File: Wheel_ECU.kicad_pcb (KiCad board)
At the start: 2 copper layers, 61 x 61 mm, 61 parts, among them J1 Conn_01x04, J2 Conn_01x04, J3 Conn_01x02, J4 Debug, J5 Conn_01x02, U1 IFX9201SG, U2 TLE4964, U3 XMC1404_F064, U4 TLE7251

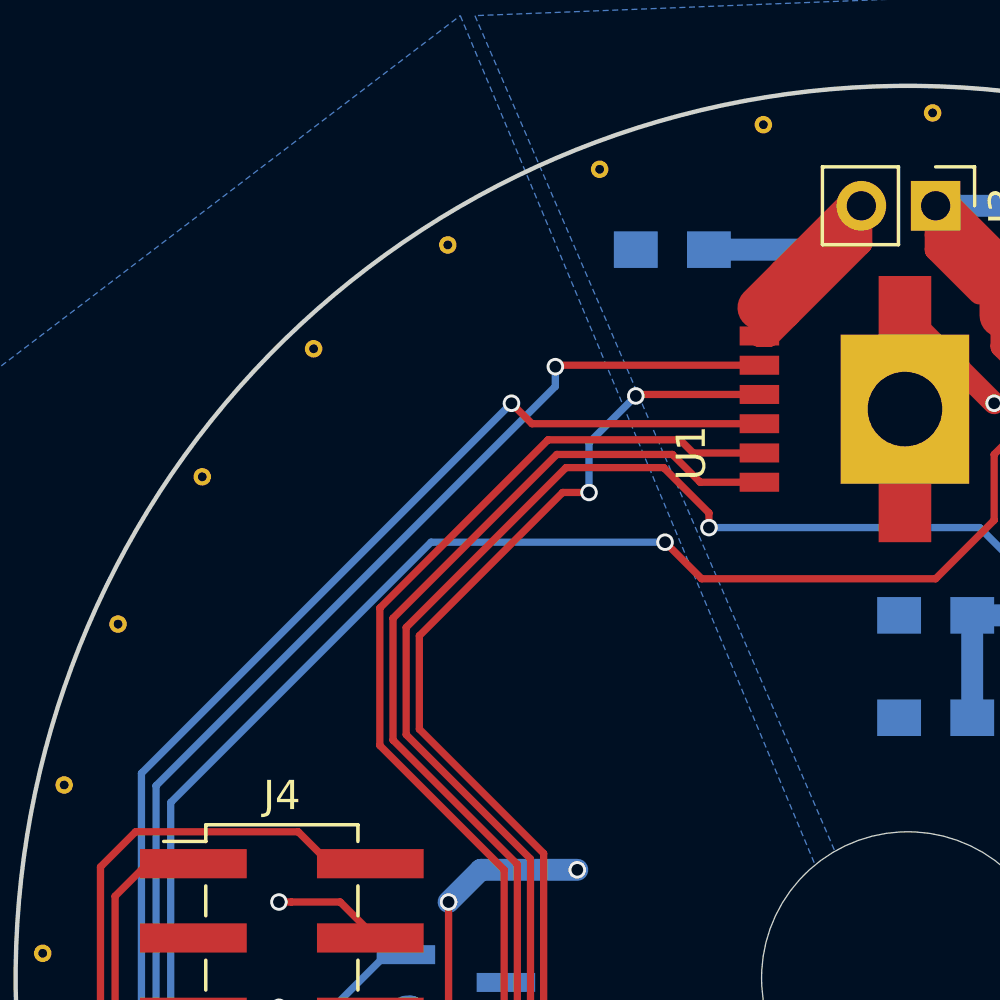
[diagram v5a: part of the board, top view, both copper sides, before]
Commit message: Add labels for the motor and debug connectors
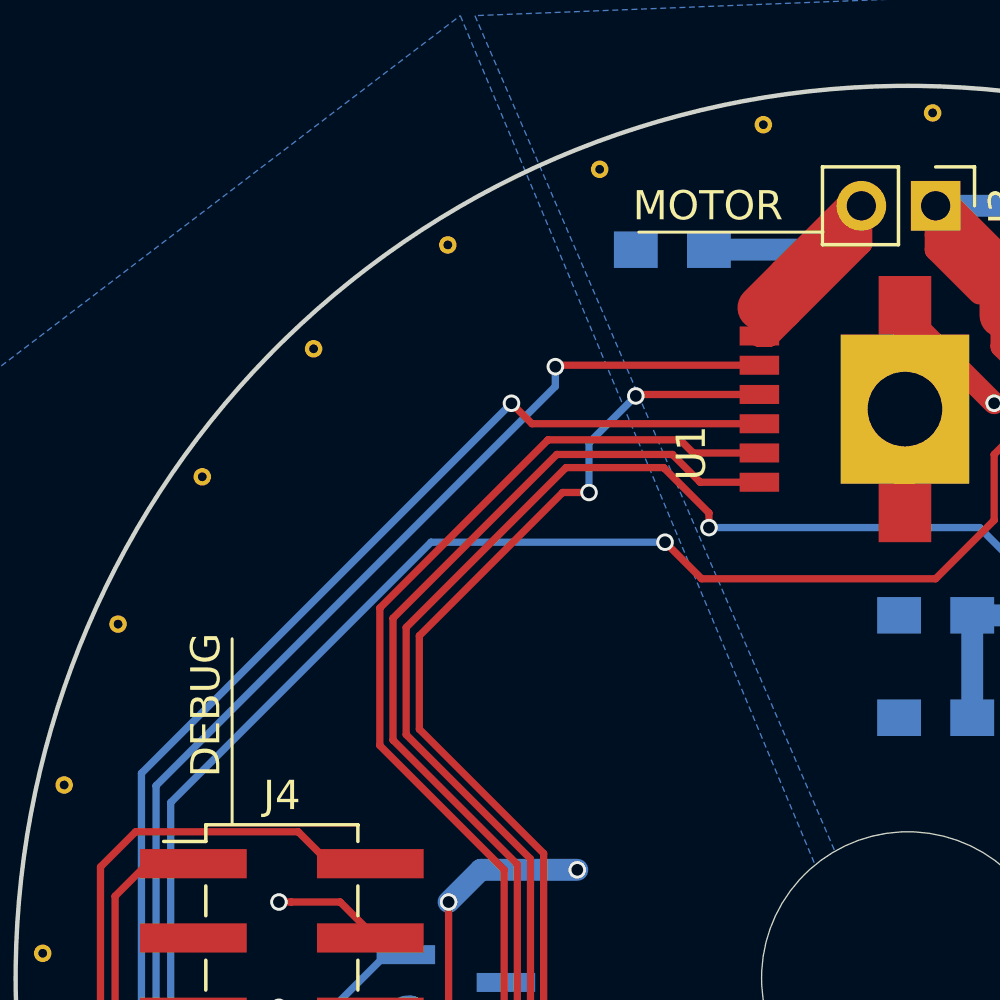
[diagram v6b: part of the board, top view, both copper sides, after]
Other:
- board text added: "DEBUG"
- board text added: "MOTOR"
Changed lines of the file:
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@@
   (general
     (thickness 1.6)
-    (drawings 6)
+    (drawings 11)
     (tracks 463)
     (zones 0)
@@
     )
   )
+  (dimension 28 (width 0.15) (layer Dwgs.User)
+    (gr_text "28,000 mm" (at 131.7 96.4) (layer Dwgs.User)
+      (effects (font (size 1 1) (thickness 0.15)))
+    )
+    (feature1 (pts (xy 145.7 98.8) (xy 145.7 97.113579)))
+    (feature2 (pts (xy 117.7 98.8) (xy 117.7 97.113579)))
+    (crossbar (pts (xy 117.7 97.7) (xy 145.7 97.7)))
+    (arrow1a (pts (xy 145.7 97.7) (xy 144.573496 98.286421)))
+    (arrow1b (pts (xy 145.7 97.7) (xy 144.573496 97.113579)))
+    (arrow2a (pts (xy 117.7 97.7) (xy 118.826504 98.286421)))
+    (arrow2b (pts (xy 117.7 97.7) (xy 118.826504 97.113579)))
+  )
+  (gr_line (start 108.7 86.8) (end 108.7 93.1) (layer F.SilkS) (width 0.1))
+  (gr_text DEBUG (at 107.8 86.6 90) (layer F.SilkS)
+    (effects (font (size 1 1) (thickness 0.1)) (justify right))
+  )
+  (gr_text MOTOR (at 122.4 72) (layer F.SilkS)
+    (effects (font (size 1 1) (thickness 0.1)) (justify left))
+  )
+  (gr_line (start 128.9 72.9) (end 122.6 72.9) (layer F.SilkS) (width 0.1))
   (gr_line (start 148.7 91.2) (end 145.4 87.9) (layer F.SilkS) (width 0.1))
   (gr_text BATT. (at 149.4 90.7 -45) (layer F.SilkS)
@@
   (gr_circle (center 131.8 98.4) (end 162.3 98.5) (layer Edge.Cuts) (width 0.15))
   (dimension 61 (width 0.3) (layer Dwgs.User)
-    (gr_text 61,000mm (at 132 58.55) (layer Dwgs.User)
+    (gr_text 61,000mm (at 131.8 58.55) (layer Dwgs.User)
       (effects (font (size 1.5 1.5) (thickness 0.3)))
     )
-    (feature1 (pts (xy 162.5 99) (xy 162.5 57.2)))
-    (feature2 (pts (xy 101.5 99) (xy 101.5 57.2)))
-    (crossbar (pts (xy 101.5 59.9) (xy 162.5 59.9)))
-    (arrow1a (pts (xy 162.5 59.9) (xy 161.373496 60.486421)))
-    (arrow1b (pts (xy 162.5 59.9) (xy 161.373496 59.313579)))
-    (arrow2a (pts (xy 101.5 59.9) (xy 102.626504 60.486421)))
-    (arrow2b (pts (xy 101.5 59.9) (xy 102.626504 59.313579)))
+    (feature1 (pts (xy 162.3 99) (xy 162.3 57.2)))
+    (feature2 (pts (xy 101.3 99) (xy 101.3 57.2)))
+    (crossbar (pts (xy 101.3 59.9) (xy 162.3 59.9)))
+    (arrow1a (pts (xy 162.3 59.9) (xy 161.173496 60.486421)))
+    (arrow1b (pts (xy 162.3 59.9) (xy 161.173496 59.313579)))
+    (arrow2a (pts (xy 101.3 59.9) (xy 102.426504 60.486421)))
+    (arrow2b (pts (xy 101.3 59.9) (xy 102.426504 59.313579)))
   )
   (gr_text "Centrifugal Fan ECU\nVersion 1.0" (at 119.3 119.2 135) (layer F.SilkS)

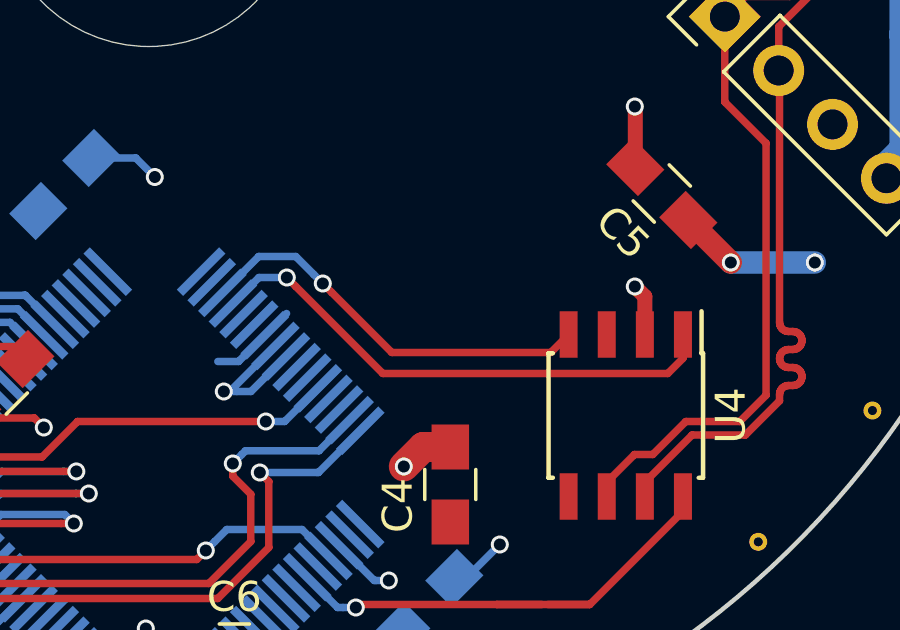
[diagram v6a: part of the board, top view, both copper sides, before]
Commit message: Move out some vias from the motor area to avoid short circuits
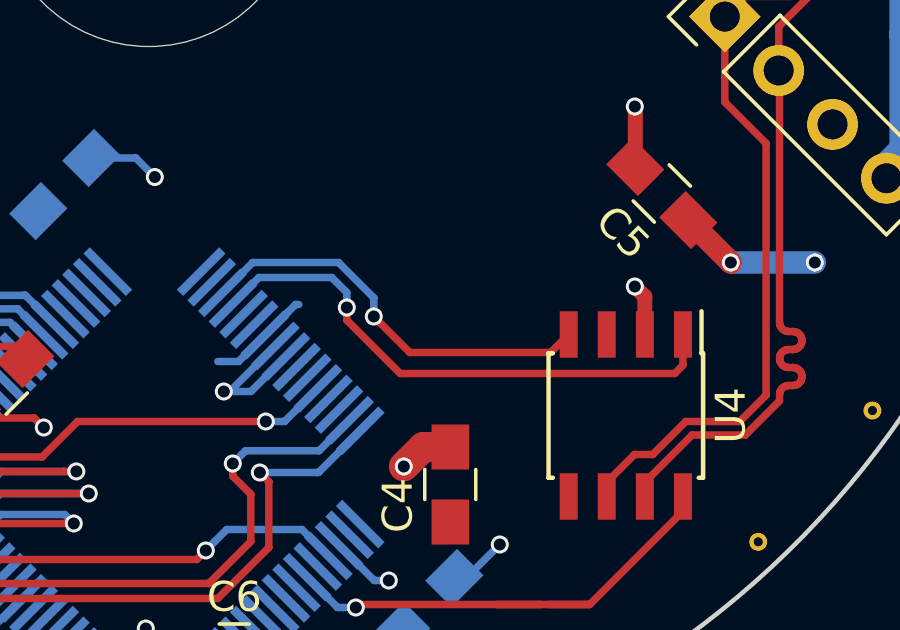
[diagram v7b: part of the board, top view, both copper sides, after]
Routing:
- net GND: track 79.0 -> 80.5 mm
- net CAN_TxD: track 17.9 -> 18.6 mm

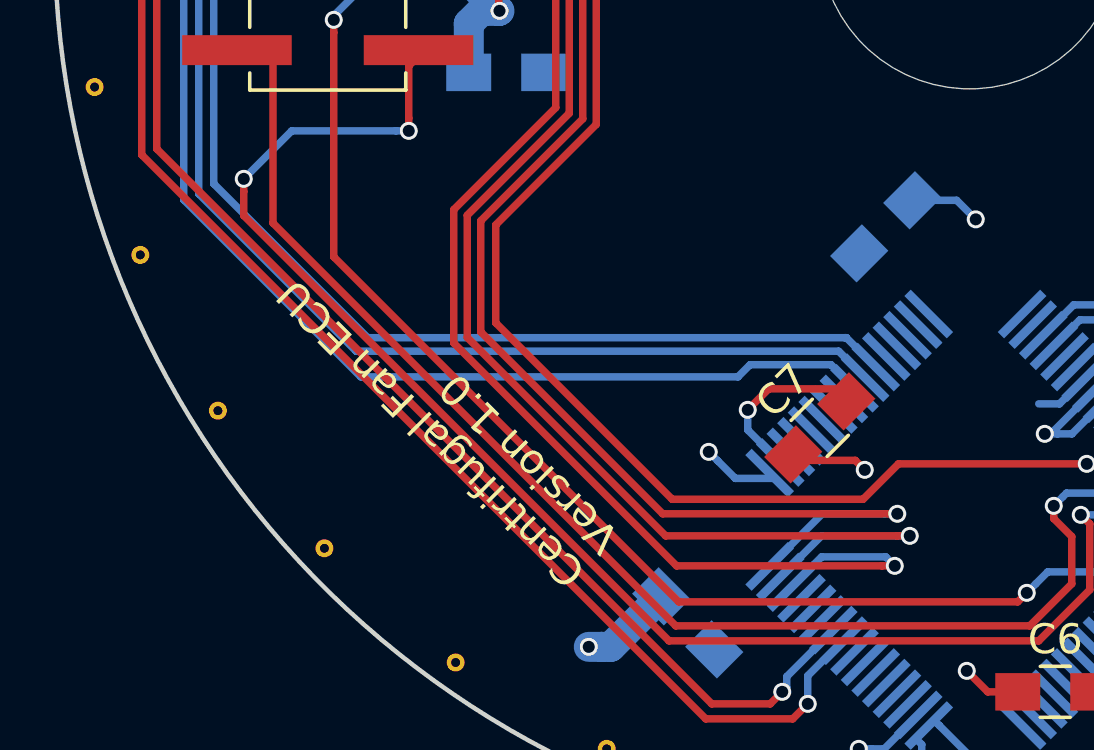
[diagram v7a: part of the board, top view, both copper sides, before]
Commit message: Add status LED
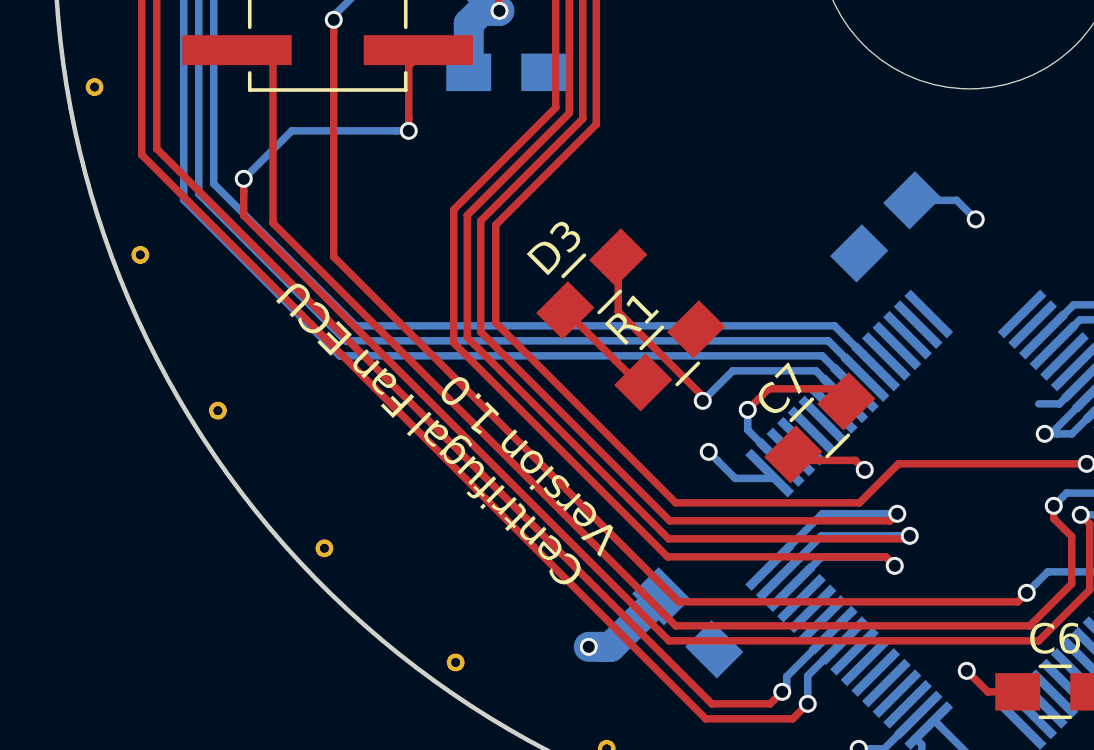
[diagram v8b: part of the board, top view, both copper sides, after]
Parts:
- added D3: LED, WheelECU:C_0805_HandSoldering, F.Cu at (119.2, 109.9)
- added R1: R, WheelECU:C_0805_HandSoldering, F.Cu at (121.8, 112.3)
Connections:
- U3 pad 8: Net-(U3-Pad8) -> STATUS_LED
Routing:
- net STATUS_LED: track 0.00 -> 11.5 mm, vias 0 -> 1
- net Net-(D3-Pad2): track 0.00 -> 3.59 mm
